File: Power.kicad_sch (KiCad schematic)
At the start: 29 parts

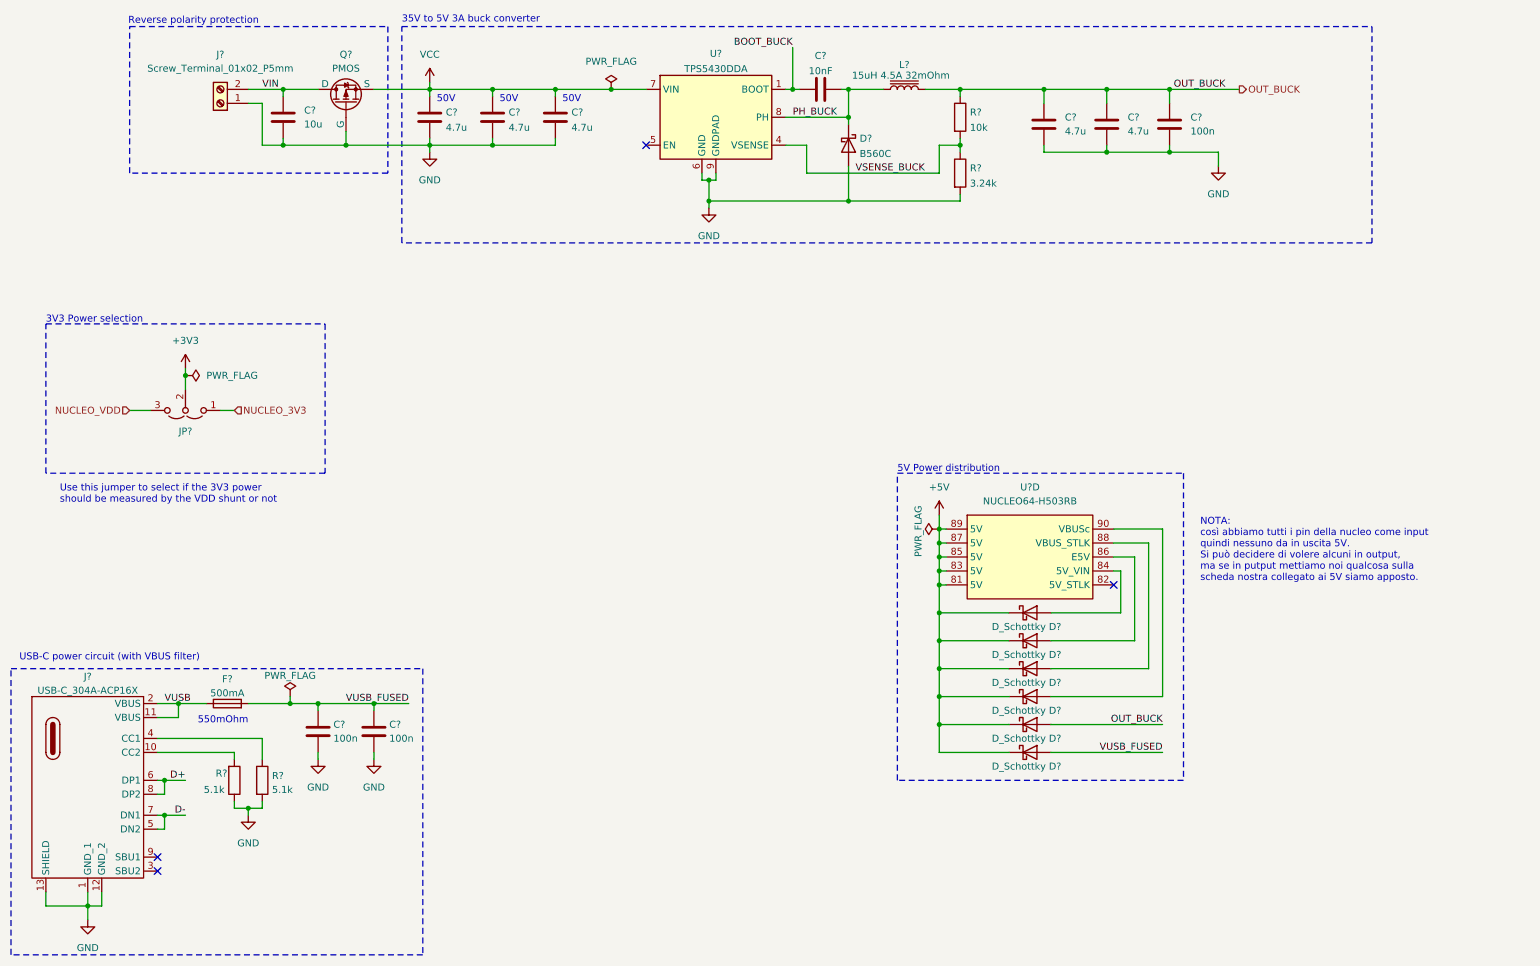
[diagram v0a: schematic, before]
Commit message: Changed some value for grouping components
Basically two resistors valued 5.1k and 5K1 have the same value
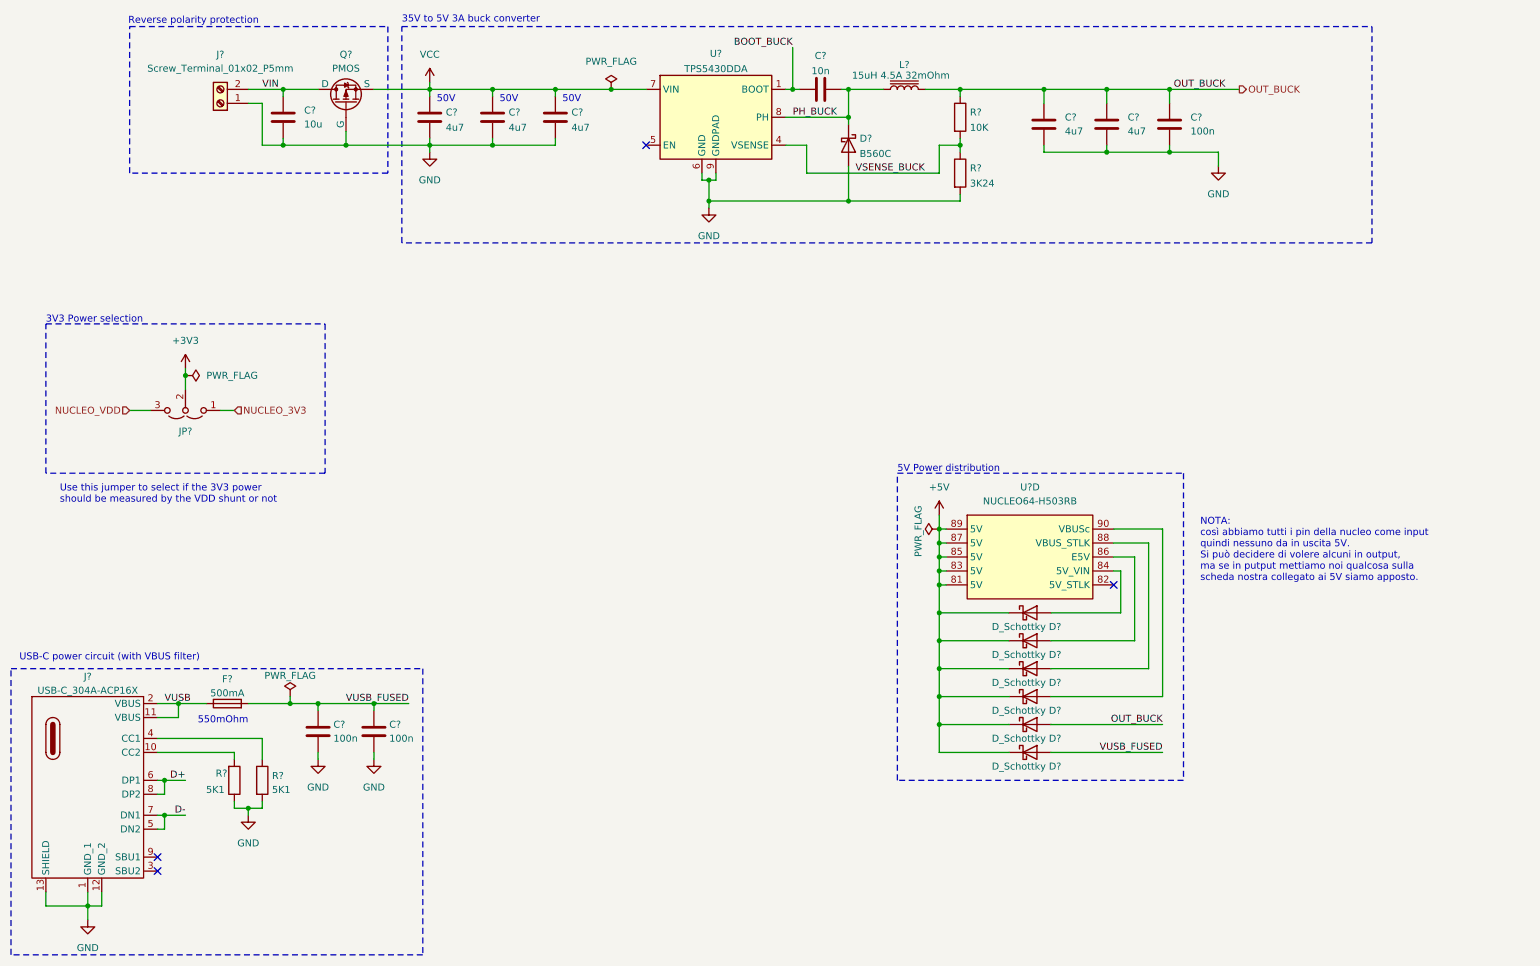
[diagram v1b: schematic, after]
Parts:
- C? (x5): value 4.7u -> 4u7
- C?: value 10nF -> 10n
- R? (x2): value 5.1k -> 5K1
- R?: value 3.24k -> 3K24
- R?: value 10k -> 10K
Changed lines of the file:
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@@
 			)
 		)
-		(property "Value" "4.7u"
+		(property "Value" "4u7"
 			(at 98.171 39.9666 0)
 			(effects
@@
 			)
 		)
-		(property "Value" "5.1k"
+		(property "Value" "5K1"
 			(at 66.548 160.4522 0)
 			(effects
@@
 			)
 		)
-		(property "Value" "10nF"
+		(property "Value" "10n"
 			(at 166.37 29.6696 90)
 			(effects
@@
 			)
 		)
-		(property "Value" "5.1k"
+		(property "Value" "5K1"
 			(at 57.9121 160.4522 0)
 			(effects
@@
 			)
 		)
-		(property "Value" "3.24k"
+		(property "Value" "3K24"
 			(at 193.548 50.1266 0)
 			(effects
@@
 			)
 		)
-		(property "Value" "4.7u"
+		(property "Value" "4u7"
 			(at 121.031 39.9666 0)
 			(effects
@@
 			)
 		)
-		(property "Value" "4.7u"
+		(property "Value" "4u7"
 			(at 109.601 39.9666 0)
 			(effects
@@
 			)
 		)
-		(property "Value" "10k"
+		(property "Value" "10K"
 			(at 193.548 39.9666 0)
 			(effects
@@
 			)
 		)
-		(property "Value" "4.7u"
+		(property "Value" "4u7"
 			(at 222.25 40.64 0)
 			(effects
@@
 			)
 		)
-		(property "Value" "4.7u"
+		(property "Value" "4u7"
 			(at 210.82 40.64 0)
 			(effects

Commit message: Referenced the shematic and started the sourcing part
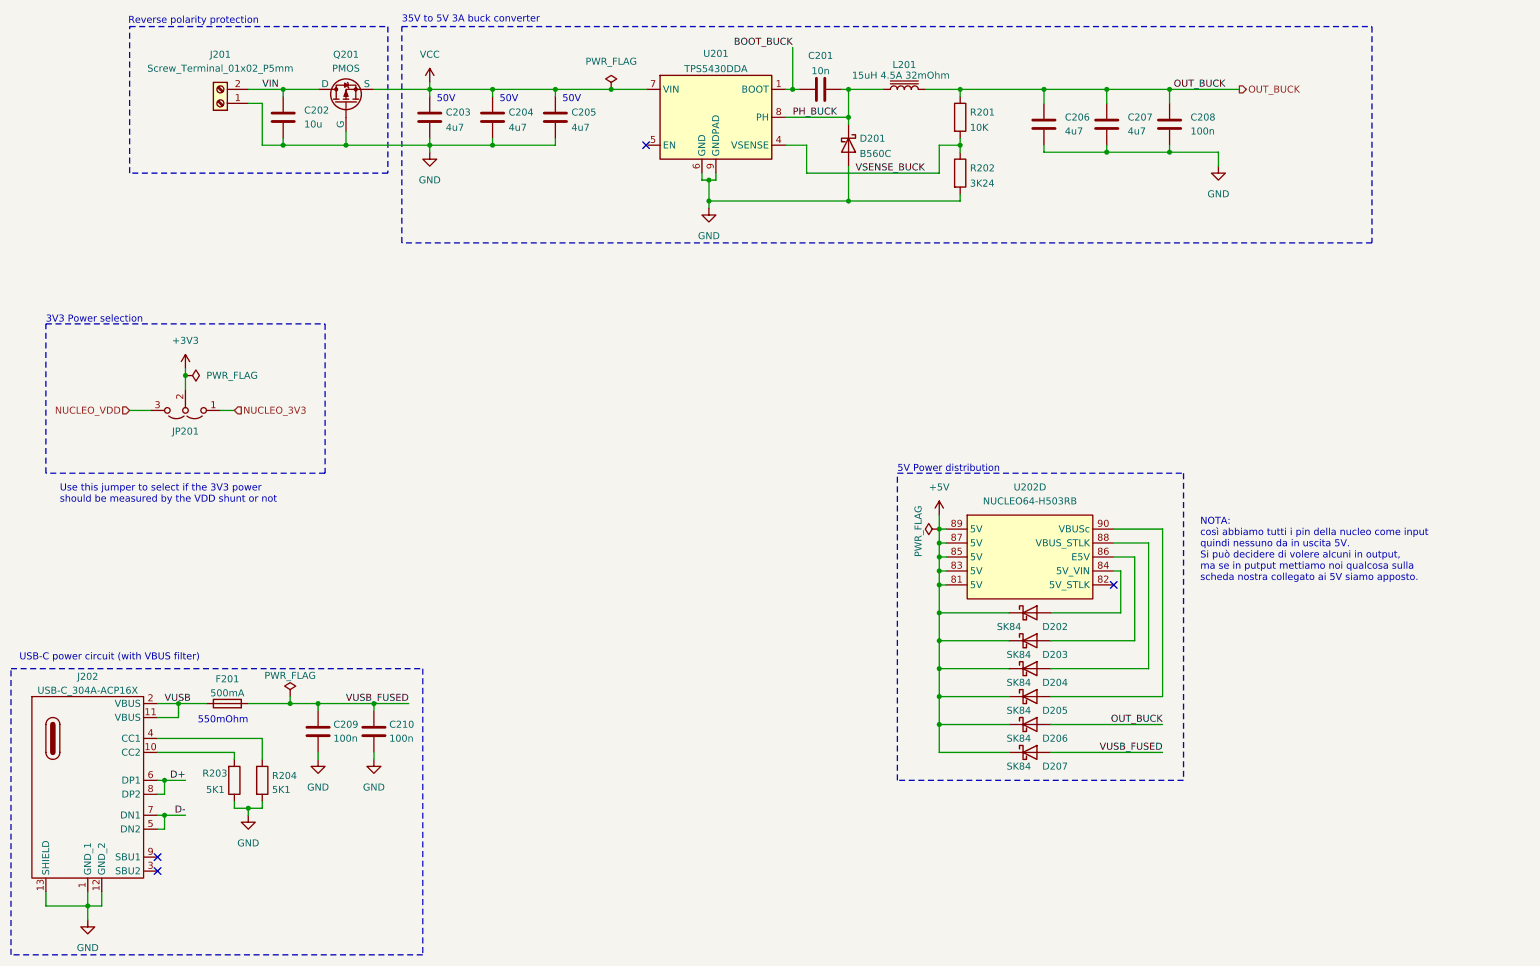
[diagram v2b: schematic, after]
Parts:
- C201: renamed from C?; footprint Capacitor_SMD:C_0805_2012Metric_Pad1.18x1.45mm_HandSolder -> Capacitor_SMD:C_0603_1608Metric_Pad1.08x0.95mm_HandSolder; LCSC (none) -> C57112
- C202: renamed from C?; footprint Capacitor_SMD:C_0805_2012Metric_Pad1.18x1.45mm_HandSolder -> Capacitor_SMD:C_0603_1608Metric_Pad1.08x0.95mm_HandSolder; LCSC (none) -> C19702
- C203, C204, C205, C206, C207: renamed from C?; footprint Capacitor_SMD:C_0805_2012Metric_Pad1.18x1.45mm_HandSolder -> Capacitor_SMD:C_0603_1608Metric_Pad1.08x0.95mm_HandSolder; LCSC (none) -> C19666
- C208, C209, C210: renamed from C?; footprint Capacitor_SMD:C_0805_2012Metric_Pad1.18x1.45mm_HandSolder -> Capacitor_SMD:C_0603_1608Metric_Pad1.08x0.95mm_HandSolder; LCSC (none) -> C14663
- D201: renamed from D?; footprint Diode_SMD:D_SMC_Handsoldering -> Diode_SMD:D_SMB-SMC_Universal_Handsoldering; LCSC (none) -> C85100
- D202, D203, D204, D205, D206, D207: renamed from D?; value D_Schottky -> SK84; footprint (none) -> Diode_SMD:D_SMB_Handsoldering; LCSC (none) -> C2922187
- F201: renamed from F?; LCSC (none) -> C151133
- JP201: renamed from JP?; LCSC (none) -> C492402
- R201: renamed from R?; footprint Resistor_SMD:R_0805_2012Metric_Pad1.20x1.40mm_HandSolder -> Resistor_SMD:R_0603_1608Metric_Pad0.98x0.95mm_HandSolder; LCSC (none) -> C25804
- R202: renamed from R?; footprint Resistor_SMD:R_0805_2012Metric_Pad1.20x1.40mm_HandSolder -> Resistor_SMD:R_0603_1608Metric_Pad0.98x0.95mm_HandSolder
- R203, R204: renamed from R?; footprint Resistor_SMD:R_0805_2012Metric_Pad1.20x1.40mm_HandSolder -> Resistor_SMD:R_0603_1608Metric_Pad0.98x0.95mm_HandSolder; LCSC (none) -> C23186
- U201: renamed from U?; LCSC (none) -> C9864
- U202: renamed from U?; now left out of the parts list
- gave numbers to parts that had none: 4

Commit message: added some lcsc code
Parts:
- J202: LCSC (none) -> C2909610
- L201: LCSC (none) -> C40000
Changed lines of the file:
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@@
 			)
 		)
-		(property "Datasheet" "~"
+		(property "Datasheet" "https://www.lcsc.com/datasheet/C40000.pdf"
 			(at 181.61 33.02 0)
 			(effects
@@
 					(size 1.27 1.27)
 				)
+			)
+		)
+		(property "LCSC" "C40000"
+			(at 181.61 33.02 90)
+			(effects
+				(font
+					(size 1.27 1.27)
+				)
+				(hide yes)
 			)
 		)
@@
 			)
 		)
+		(property "LCSC" "C2909610"
+			(at 33.02 158.75 0)
+			(effects
+				(font
+					(size 1.27 1.27)
+				)
+				(hide yes)
+			)
+		)

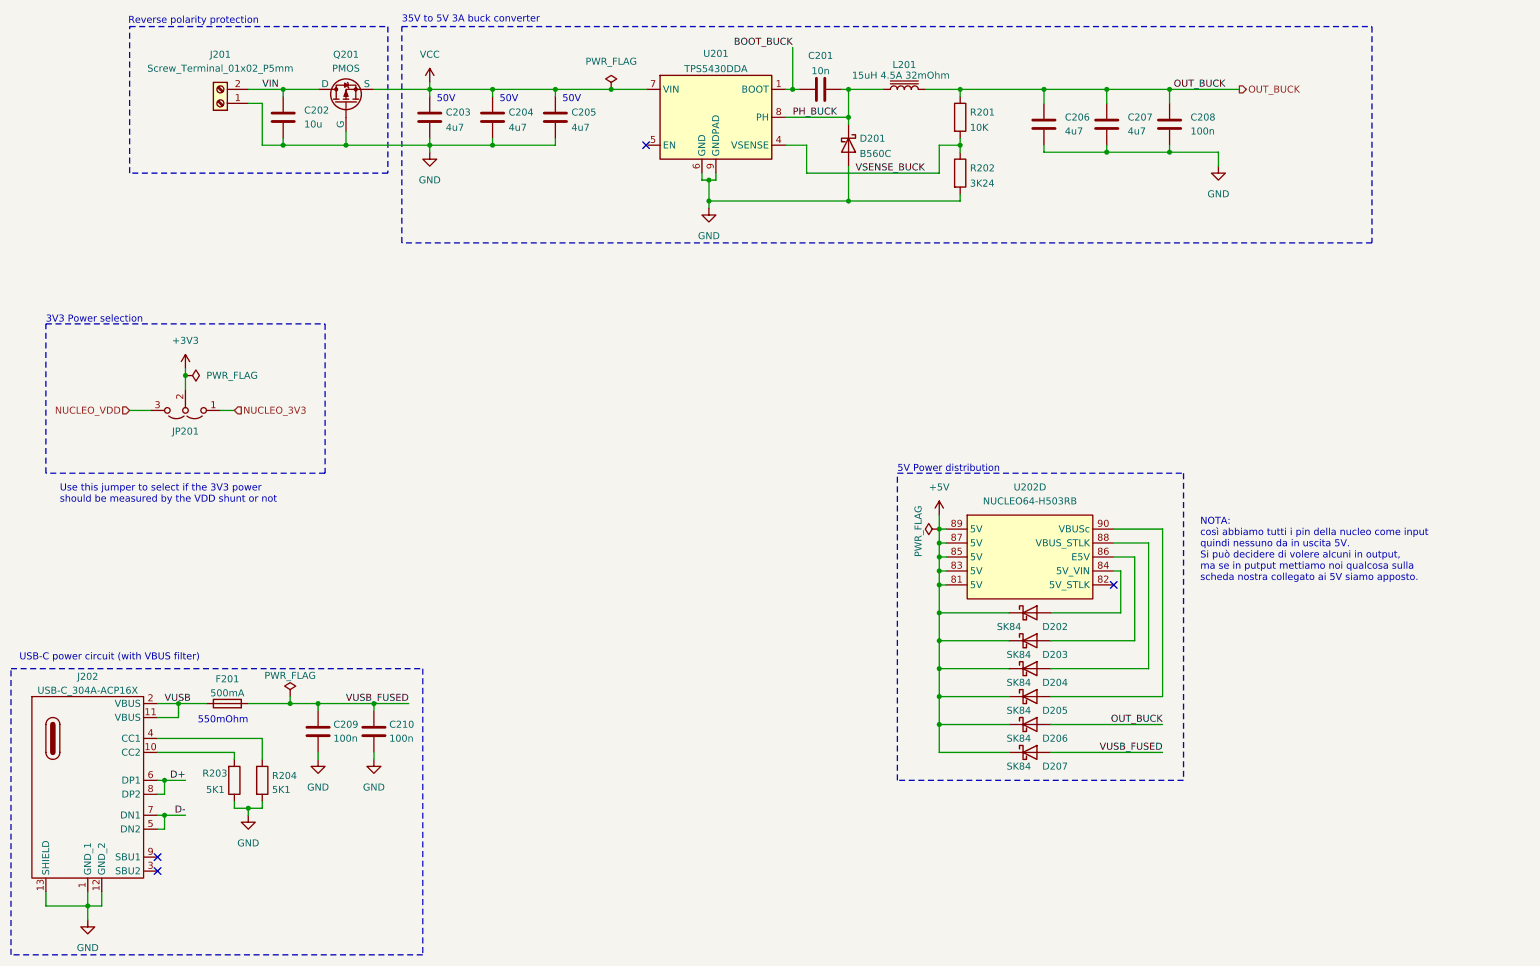
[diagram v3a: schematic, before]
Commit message: added some lcsc codes, changed reverse voltage protection with a diode
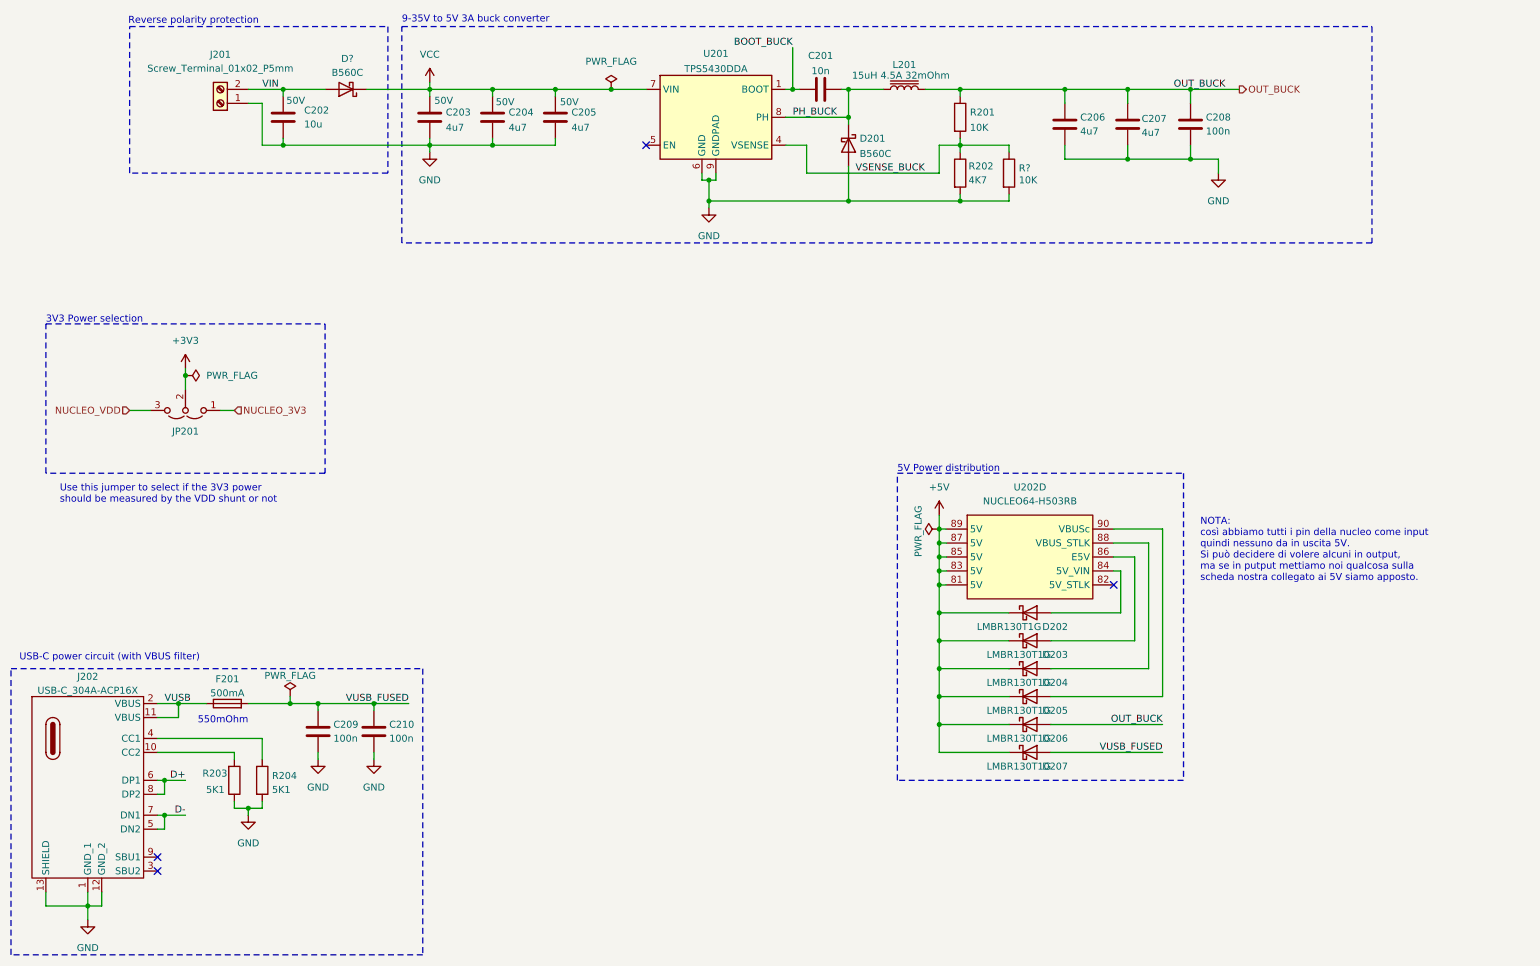
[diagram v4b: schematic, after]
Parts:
- removed Q201: PMOS, symbol Simulation_SPICE:PMOS
- added D?: B560C, Diode_SMD:D_SMB-SMC_Universal_Handsoldering, symbol Device:D_Schottky
- added R?: 10K, Resistor_SMD:R_0603_1608Metric_Pad0.98x0.95mm_HandSolder, symbol Device:R
- C202, C203, C204, C205: Voltage (none) -> 50V
- D202, D203, D204, D205, D206, D207: value SK84 -> LMBR130T1G; footprint Diode_SMD:D_SMB_Handsoldering -> Diode_SMD:D_SOD-123; LCSC C2922187 -> C48974
- R202: value 3K24 -> 4K7; LCSC (none) -> C4177
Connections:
- net GND: now also R?.2
- net VCC: now also D?.1 (K)
- net VIN: now also D?.2 (A)
- net VSENSE_BUCK: now also R?.1
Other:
- note added: "9-35V to 5V 3A buck converter"
- note removed: "35V to 5V 3A buck converter"
- note removed: "50V"
- moved on the sheet: C206, C207, C208

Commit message: added some lcsc PN, and uniformed some resistors values to reduce BOM count
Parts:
- J201: footprint (none) -> TerminalBlock:TerminalBlock_MaiXu_MX126-5.0-02P_1x02_P5.00mm; LCSC (none) -> C474881
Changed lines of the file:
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@@
 			)
 		)
-		(property "Footprint" ""
+		(property "Footprint" "TerminalBlock:TerminalBlock_MaiXu_MX126-5.0-02P_1x02_P5.00mm"
 			(at 57.15 35.56 0)
 			(effects
@@
 			(at 57.15 35.56 0)
 			(effects
+				(font
+					(size 1.27 1.27)
+				)
+				(hide yes)
+			)
+		)
+		(property "LCSC" "C474881"
+			(at 57.15 35.56 0)
+			(effects
